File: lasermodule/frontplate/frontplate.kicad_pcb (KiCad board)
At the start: 2 copper layers, 25.2 x 55.1 mm, 2 parts

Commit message: simplified loading in freecad, updated pcbs
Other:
- board text added: "PCB3D_BR_frontplate"
- board text added: "PCB3D_TL_frontplate"

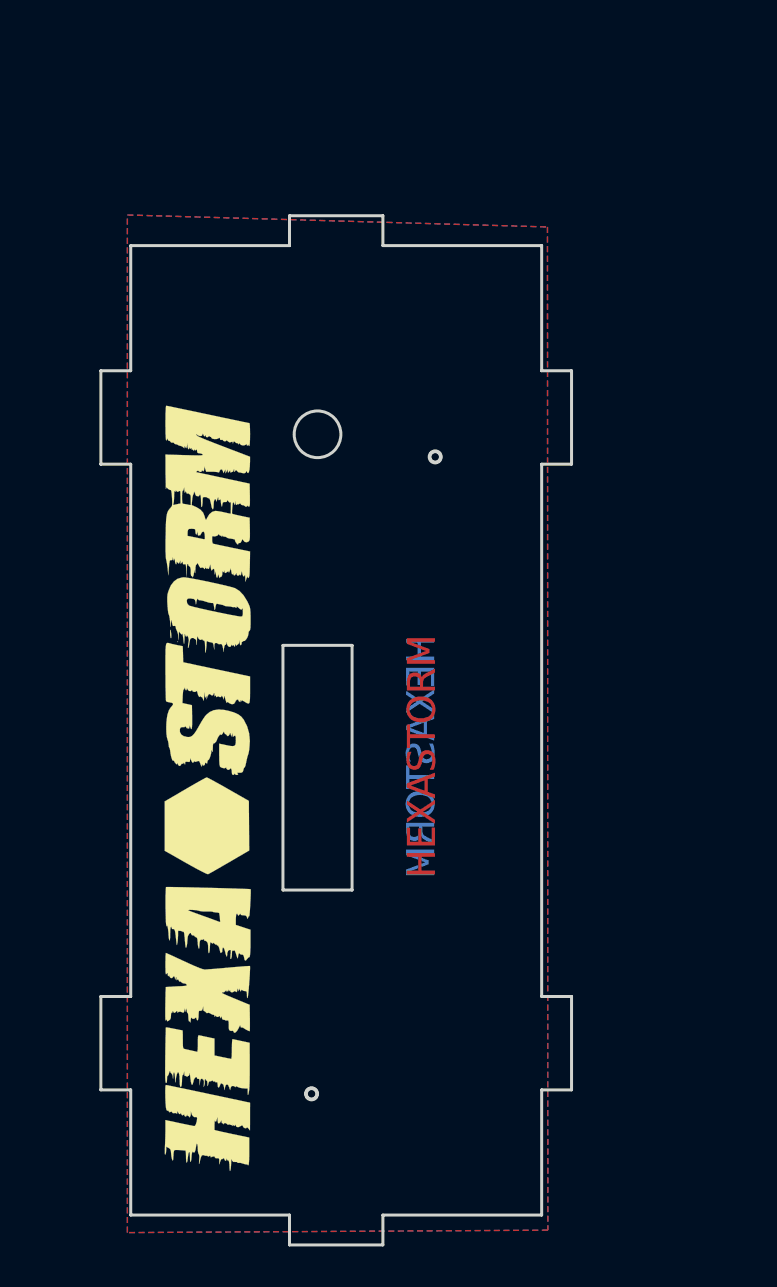
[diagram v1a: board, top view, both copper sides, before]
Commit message: pcbs can be rendered
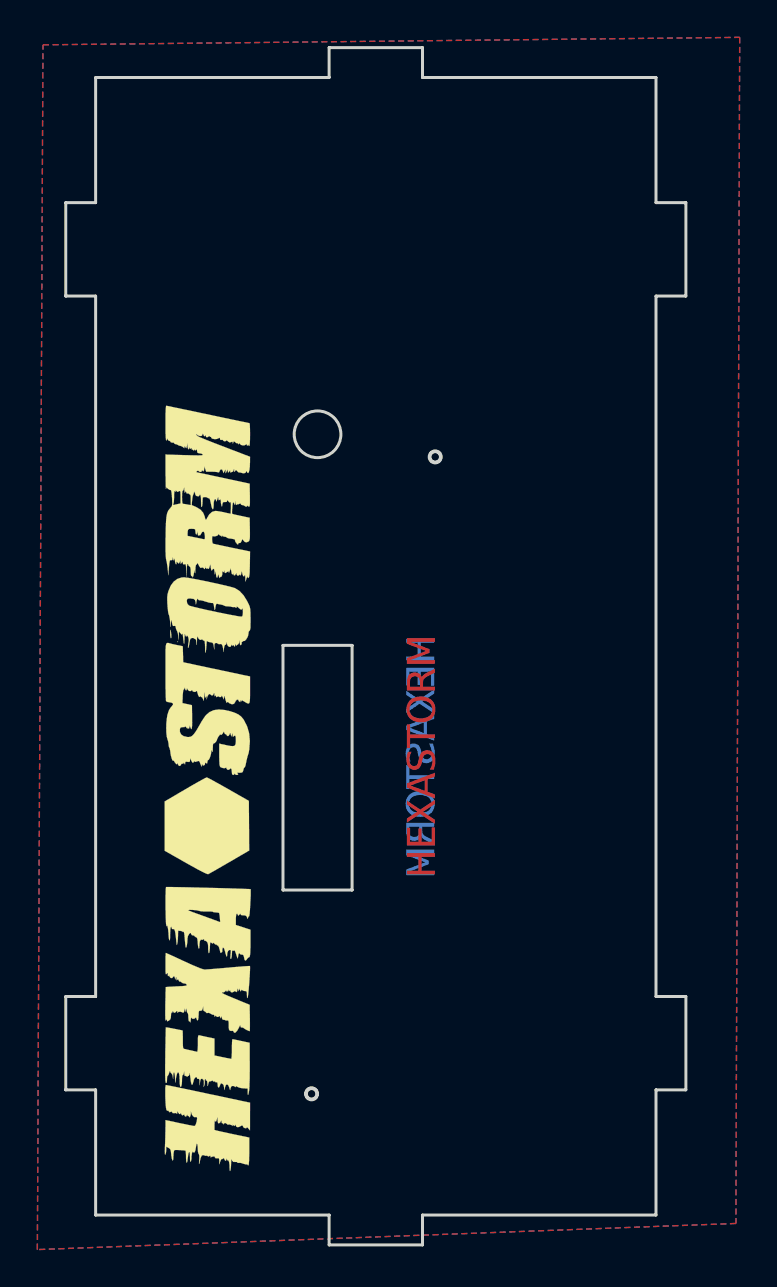
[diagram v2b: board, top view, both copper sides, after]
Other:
- board size 25.2 x 55.1 mm -> 33.2 x 64.1 mm
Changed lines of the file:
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@@
       (stroke (width 0.01) (type solid)) (fill solid) (layer "B.SilkS"))
   )
-  (gr_line (start 166.114 75.999) (end 166.114 82.7)
+  (gr_line (start 172.2345 116.1995) (end 173.8345 116.1995)
     (stroke (width 0.16) (type solid)) (layer "Edge.Cuts"))
-  (gr_line (start 152.614 75.999) (end 152.614 74.4)
+  (gr_line (start 173.8345 116.1995) (end 173.8345 121.1995)
     (stroke (width 0.16) (type solid)) (layer "Edge.Cuts"))
-  (gr_line (start 166.114 87.7) (end 166.114 116.2)
+  (gr_line (start 172.2345 66.9995) (end 172.2345 73.6995)
     (stroke (width 0.16) (type solid)) (layer "Edge.Cuts"))
-  (gr_line (start 152.614 74.4) (end 157.614 74.4)
+  (gr_line (start 142.2345 121.1995) (end 140.6345 121.1995)
     (stroke (width 0.16) (type solid)) (layer "Edge.Cuts"))
-  (gr_line (start 155.964 97.4) (end 152.264 97.4)
+  (gr_line (start 172.2345 73.6995) (end 173.8345 73.6995)
     (stroke (width 0.16) (type solid)) (layer "Edge.Cuts"))
-  (gr_line (start 166.114 127.9) (end 157.614 127.9)
+  (gr_line (start 152.2645 110.4995) (end 155.9645 110.4995)
     (stroke (width 0.16) (type solid)) (layer "Edge.Cuts"))
-  (gr_line (start 152.264 110.499) (end 155.964 110.499)
+  (gr_line (start 140.6345 121.1995) (end 140.6345 116.1995)
     (stroke (width 0.16) (type solid)) (layer "Edge.Cuts"))
-  (gr_line (start 157.614 75.999) (end 166.114 75.999)
+  (gr_line (start 155.9645 97.3995) (end 152.2645 97.3995)
     (stroke (width 0.16) (type solid)) (layer "Edge.Cuts"))
-  (gr_line (start 142.514 116.2) (end 144.114 116.2)
+  (gr_line (start 154.7345 66.9995) (end 154.7345 65.3995)
     (stroke (width 0.16) (type solid)) (layer "Edge.Cuts"))
-  (gr_line (start 144.114 127.9) (end 152.614 127.9)
+  (gr_line (start 142.2345 78.6995) (end 140.6345 78.6995)
     (stroke (width 0.16) (type solid)) (layer "Edge.Cuts"))
-  (gr_line (start 166.114 116.2) (end 167.714 116.2)
+  (gr_line (start 152.2645 97.3995) (end 152.2645 110.4995)
     (stroke (width 0.16) (type solid)) (layer "Edge.Cuts"))
-  (gr_line (start 144.114 87.7) (end 144.114 116.2)
+  (gr_line (start 159.7345 129.4995) (end 154.7345 129.4995)
     (stroke (width 0.16) (type solid)) (layer "Edge.Cuts"))
-  (gr_line (start 142.514 87.7) (end 142.514 82.7)
+  (gr_line (start 142.2345 66.9995) (end 154.7345 66.9995)
     (stroke (width 0.16) (type solid)) (layer "Edge.Cuts"))
-  (gr_line (start 144.114 87.7) (end 142.514 87.7)
+  (gr_line (start 173.8345 73.6995) (end 173.8345 78.6995)
     (stroke (width 0.16) (type solid)) (layer "Edge.Cuts"))
-  (gr_line (start 144.114 121.2) (end 144.114 127.9)
+  (gr_line (start 155.9645 110.4995) (end 155.9645 97.3995)
     (stroke (width 0.16) (type solid)) (layer "Edge.Cuts"))
-  (gr_line (start 166.114 82.7) (end 167.714 82.7)
+  (gr_line (start 154.7345 129.4995) (end 154.7345 127.8995)
     (stroke (width 0.16) (type solid)) (layer "Edge.Cuts"))
-  (gr_line (start 152.614 129.5) (end 152.614 127.9)
+  (gr_line (start 142.2345 127.8995) (end 154.7345 127.8995)
     (stroke (width 0.16) (type solid)) (layer "Edge.Cuts"))
-  (gr_line (start 166.114 121.2) (end 166.114 127.9)
+  (gr_line (start 172.2345 121.1995) (end 172.2345 127.8995)
     (stroke (width 0.16) (type solid)) (layer "Edge.Cuts"))
-  (gr_line (start 152.264 97.4) (end 152.264 110.499)
+  (gr_line (start 142.2345 78.6995) (end 142.2345 116.1995)
     (stroke (width 0.16) (type solid)) (layer "Edge.Cuts"))
-  (gr_line (start 167.714 116.2) (end 167.714 121.2)
+  (gr_line (start 173.8345 78.6995) (end 172.2345 78.6995)
     (stroke (width 0.16) (type solid)) (layer "Edge.Cuts"))
-  (gr_line (start 157.614 129.5) (end 152.614 129.5)
+  (gr_line (start 159.7345 127.8995) (end 159.7345 129.4995)
     (stroke (width 0.16) (type solid)) (layer "Edge.Cuts"))
-  (gr_line (start 155.964 110.499) (end 155.964 97.4)
+  (gr_line (start 154.7345 65.3995) (end 159.7345 65.3995)
     (stroke (width 0.16) (type solid)) (layer "Edge.Cuts"))
-  (gr_line (start 144.114 121.2) (end 142.514 121.2)
+  (gr_line (start 172.2345 127.8995) (end 159.7345 127.8995)
     (stroke (width 0.16) (type solid)) (layer "Edge.Cuts"))
-  (gr_line (start 157.614 74.4) (end 157.614 75.999)
+  (gr_line (start 142.2345 66.9995) (end 142.2345 73.6995)
     (stroke (width 0.16) (type solid)) (layer "Edge.Cuts"))
-  (gr_line (start 144.114 75.999) (end 144.114 82.7)
+  (gr_line (start 173.8345 121.1995) (end 172.2345 121.1995)
     (stroke (width 0.16) (type solid)) (layer "Edge.Cuts"))
-  (gr_line (start 142.514 121.2) (end 142.514 116.2)
+  (gr_line (start 140.6345 73.6995) (end 142.2345 73.6995)
     (stroke (width 0.16) (type solid)) (layer "Edge.Cuts"))
-  (gr_line (start 167.714 121.2) (end 166.114 121.2)
+  (gr_line (start 140.6345 116.1995) (end 142.2345 116.1995)
     (stroke (width 0.16) (type solid)) (layer "Edge.Cuts"))
-  (gr_line (start 157.614 127.9) (end 157.614 129.5)
+  (gr_line (start 140.6345 78.6995) (end 140.6345 73.6995)
     (stroke (width 0.16) (type solid)) (layer "Edge.Cuts"))
-  (gr_circle (center 154.114 86.1) (end 152.864 86.1)
+  (gr_line (start 142.2345 121.1995) (end 142.2345 127.8995)
+    (stroke (width 0.16) (type solid)) (layer "Edge.Cuts"))
+  (gr_line (start 159.7345 65.3995) (end 159.7345 66.9995)
+    (stroke (width 0.16) (type solid)) (layer "Edge.Cuts"))
+  (gr_line (start 159.7345 66.9995) (end 172.2345 66.9995)
+    (stroke (width 0.16) (type solid)) (layer "Edge.Cuts"))
+  (gr_circle (center 154.1145 86.0995) (end 152.8645 86.0995)
     (stroke (width 0.16) (type solid)) (fill none) (layer "Edge.Cuts"))
-  (gr_line (start 142.514 82.7) (end 144.114 82.7)
-    (stroke (width 0.16) (type solid)) (layer "Edge.Cuts"))
-  (gr_line (start 144.114 75.999) (end 152.614 75.999)
-    (stroke (width 0.16) (type solid)) (layer "Edge.Cuts"))
-  (gr_line (start 167.714 87.7) (end 166.114 87.7)
-    (stroke (width 0.16) (type solid)) (layer "Edge.Cuts"))
-  (gr_line (start 167.714 82.7) (end 167.714 87.7)
+  (gr_line (start 172.2345 78.6995) (end 172.2345 116.1995)
     (stroke (width 0.16) (type solid)) (layer "Edge.Cuts"))
   (gr_text "HEXASTORM" (at 159.7045 103.3395 90) (layer "F.Cu")
@@
     (effects (font (size 1 1) (thickness 0.15)))
   )
-  (gr_text "PCB3D_TL_frontplate" (at 143.9545 73.4695) (layer "Cmts.User")
+  (gr_text "PCB3D_TL_frontplate" (at 137.2145 64.3495) (layer "Cmts.User")
     (effects (font (size 1 1) (thickness 0.15)) (justify left bottom))
   )
-  (gr_text "PCB3D_BR_frontplate" (at 151.5745 131.8895) (layer "Cmts.User")
+  (gr_text "PCB3D_BR_frontplate" (at 177.1145 130.4495) (layer "Cmts.User")
     (effects (font (size 1 1) (thickness 0.15)) (justify left bottom))
   )
@@
     (polygon
       (pts
-        (xy 166.4445 128.7095)
-        (xy 143.9345 128.8395)
-        (xy 143.9345 74.3595)
-        (xy 166.4245 74.9995)
+        (xy 176.5145 128.3495)
+        (xy 139.1145 129.7495)
+        (xy 139.4145 65.2495)
+        (xy 176.7145 64.8495)
       )
     )

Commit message: changed position logos
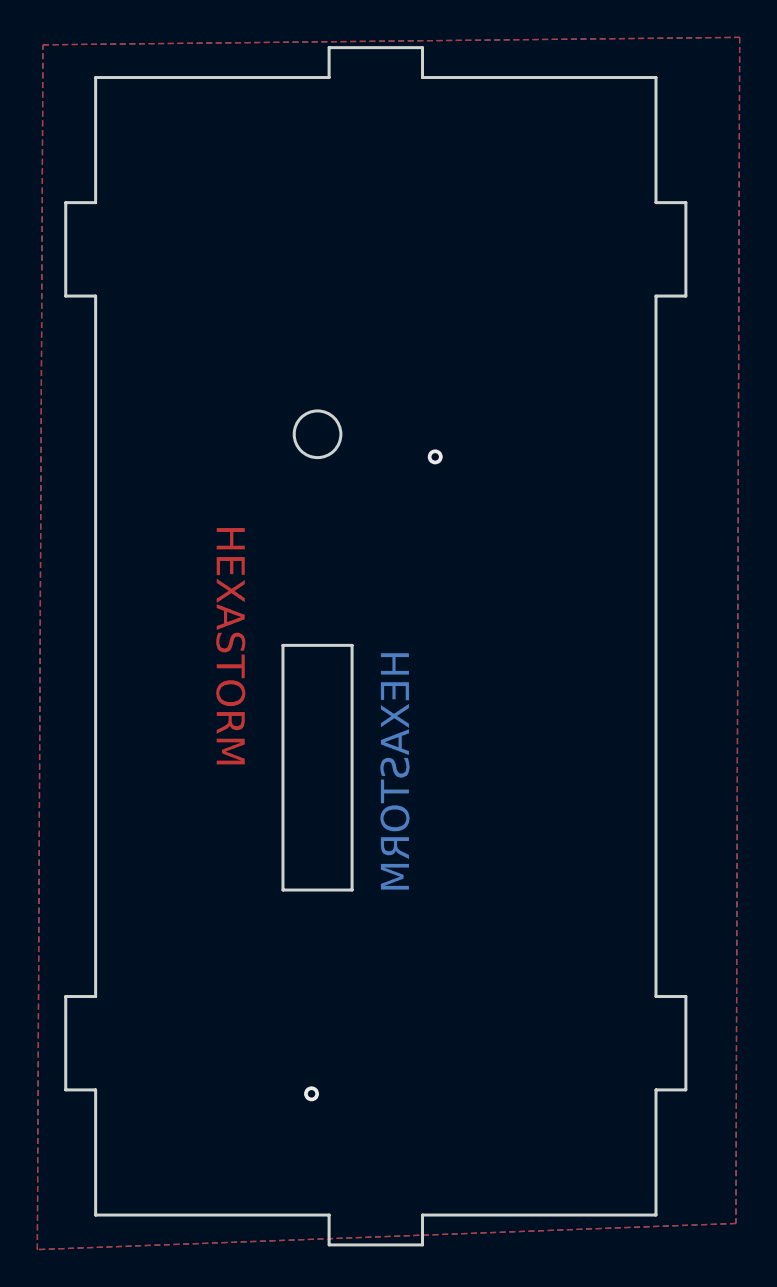
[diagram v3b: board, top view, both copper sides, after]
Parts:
- removed L1, L2: Logo_Open_Hardware_Large, footprints:hexastorm
